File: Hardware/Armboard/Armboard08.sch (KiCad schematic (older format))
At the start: 0 parts

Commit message: Added serial pins, limit switches, titles, and indicators
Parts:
- added Conn? (x3): Molex_SL_03, symbol MRDT_Connectors:Molex_SL_03
- added D? (x6): LED, symbol Device:LED
- added R? (x6): 500, symbol Device:R
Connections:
- new net: D?.2 (A), R?.2 (x6)
- new net GND: Conn?.2, Conn?.2, Conn?.2, D?.1 (K), D?.1 (K), D?.1 (K), D?.1 (K), D?.1 (K), D?.1 (K)
- new net Rx_1_Tiva: Conn?.1, R?.1
- new net Rx_2_Tiva: Conn?.1, R?.1
- new net Rx_3_Tiva: Conn?.1, R?.1
- new net Tx_1_Tiva: Conn?.3, R?.1
- new net Tx_2_Tiva: Conn?.3, R?.1
- new net Tx_3_Tiva: Conn?.3, R?.1
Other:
- note added: "Purple"
- note added: "Serial Pins"

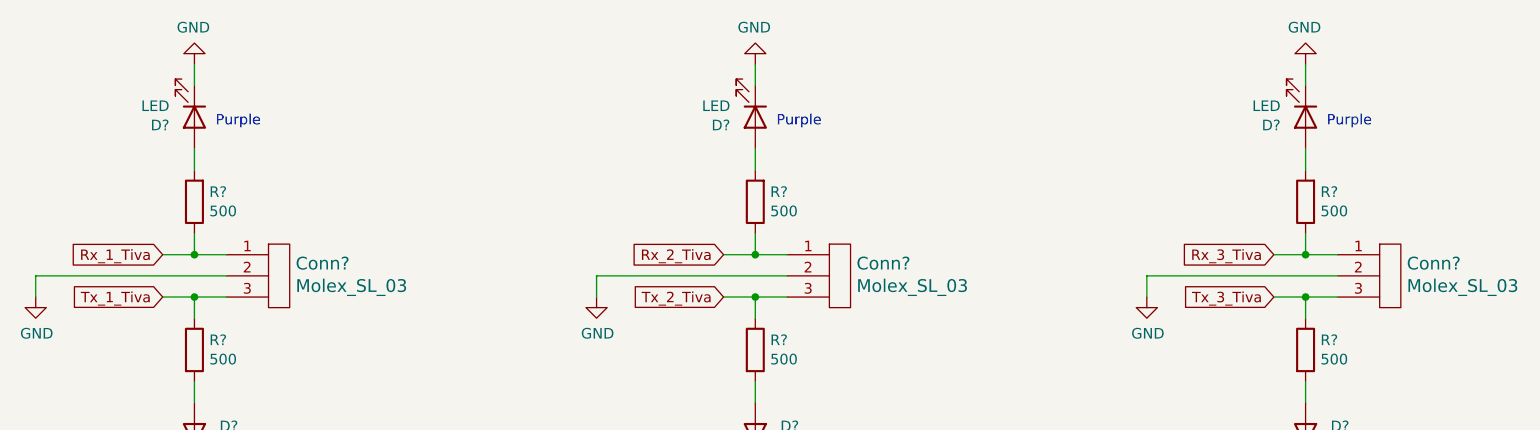
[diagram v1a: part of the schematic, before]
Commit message: Formatted GNDs and added motor toggle buttons
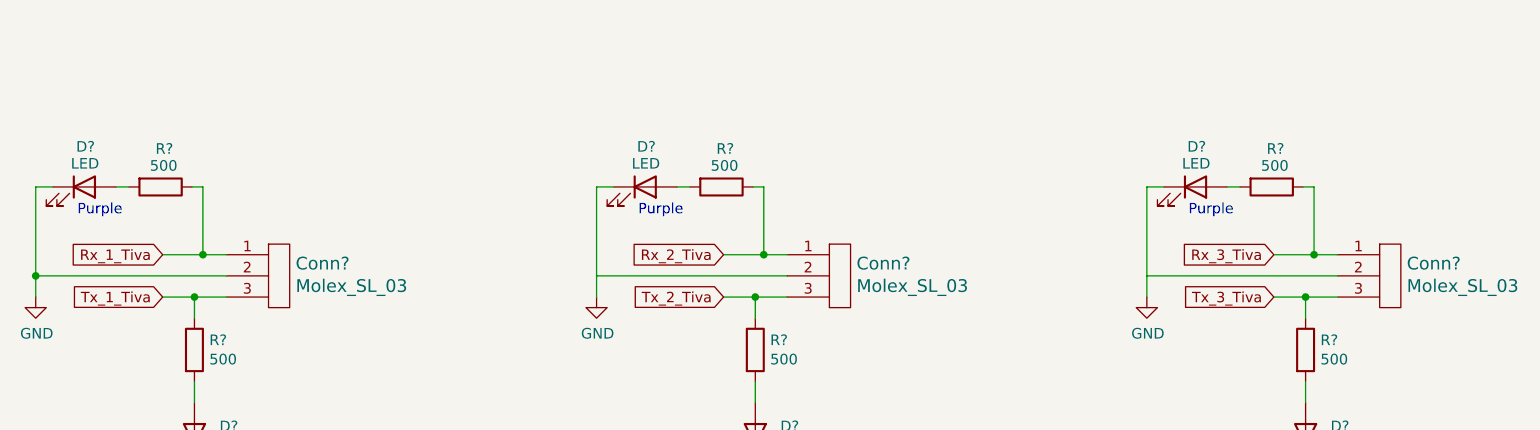
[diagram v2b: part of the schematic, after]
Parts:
- removed D? (x2): LED, symbol Device:LED
- removed R? (x2): 500, symbol Device:R
- added D? (x2): LED, symbol Device:LED
- added R? (x2): 500, symbol Device:R
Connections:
- net GND: now also D?.1 (K), D?.1 (K)
- net Rx_2_Tiva: now also R?.1
- net Rx_3_Tiva: now also R?.1
- new net: D?.2 (A), R?.2 (x2)
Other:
- moved on the sheet: D?, R?
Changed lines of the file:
@@
 Tx_1_Tiva
-Wire Wire Line
-	2950 3550 2800 3550
 Wire Wire Line
 	2950 3750 2800 3750
@@
 L Device:R R?
 U 1 1 5F88CC5B
-P 2800 3300
-F 0 "R?" H 2730 3254 50  0000 R CNN
-F 1 "500" H 2730 3345 50  0000 R CNN
-F 2 "" V 2730 3300 50  0001 C CNN
-F 3 "~" H 2800 3300 50  0001 C CNN
-	1    2800 3300
-	-1   0    0    1
+P 2640 3230
+F 0 "R?" V 2460 3290 50  0000 R CNN
+F 1 "500" V 2540 3310 50  0000 R CNN
+F 2 "" V 2570 3230 50  0001 C CNN
+F 3 "~" H 2640 3230 50  0001 C CNN
+	1    2640 3230
+	0    1    1    0
 $EndComp
 $Comp
 L Device:LED D?
 U 1 1 5F88CC61
-P 2800 2900
-F 0 "D?" V 2839 2782 50  0000 R CNN
-F 1 "LED" V 2748 2782 50  0000 R CNN
-F 2 "" H 2800 2900 50  0001 C CNN
-F 3 "~" H 2800 2900 50  0001 C CNN
-	1    2800 2900
-	0    1    1    0
-$EndComp
-$Comp
-L power:GND #PWR?
-U 1 1 5F88CC67
-P 2800 2650
-F 0 "#PWR?" H 2800 2400 50  0001 C CNN
-F 1 "GND" H 2805 2477 50  0000 C CNN
-F 2 "" H 2800 2650 50  0001 C CNN
-F 3 "" H 2800 2650 50  0001 C CNN
-	1    2800 2650
-	-1   0    0    1
+P 2280 3230
+F 0 "D?" H 2330 3420 50  0000 R CNN
+F 1 "LED" H 2350 3340 50  0000 R CNN
+F 2 "" H 2280 3230 50  0001 C CNN
+F 3 "~" H 2280 3230 50  0001 C CNN
+	1    2280 3230
+	1    0    0    -1
 $EndComp
 Wire Wire Line
@@
 Wire Wire Line
 	2800 4650 2800 4550
-Wire Wire Line
-	2800 3450 2800 3550
-Connection ~ 2800 3550
-Wire Wire Line
-	2800 3550 2650 3550
-Wire Wire Line
-	2800 2750 2800 2650
-Wire Wire Line
-	2800 3050 2800 3150
 Text Notes 2450 4450 0    49   ~ 0
 Purple
-Text Notes 2900 2950 0    49   ~ 0
+Text Notes 2460 3370 2    49   ~ 0
 Purple
 $Comp
@@
 Tx_2_Tiva
 Wire Wire Line
-	5600 3550 5450 3550
-Wire Wire Line
 	5600 3750 5450 3750
 Wire Wire Line
@@
 	1    0    0    -1
 $EndComp
-$Comp
-L Device:R R?
-U 1 1 5F88E69D
-P 5450 3300
-F 0 "R?" H 5380 3254 50  0000 R CNN
-F 1 "500" H 5380 3345 50  0000 R CNN
-F 2 "" V 5380 3300 50  0001 C CNN
-F 3 "~" H 5450 3300 50  0001 C CNN
-	1    5450 3300
-	-1   0    0    1
-$EndComp
-$Comp
-L Device:LED D?
-U 1 1 5F88E6A3
-P 5450 2900
-F 0 "D?" V 5489 2782 50  0000 R CNN
-F 1 "LED" V 5398 2782 50  0000 R CNN
-F 2 "" H 5450 2900 50  0001 C CNN
-F 3 "~" H 5450 2900 50  0001 C CNN
-	1    5450 2900
-	0    1    1    0
-$EndComp
-$Comp
-L power:GND #PWR?
-U 1 1 5F88E6A9
-P 5450 2650
-F 0 "#PWR?" H 5450 2400 50  0001 C CNN
-F 1 "GND" H 5455 2477 50  0000 C CNN
-F 2 "" H 5450 2650 50  0001 C CNN
-F 3 "" H 5450 2650 50  0001 C CNN
-	1    5450 2650
-	-1   0    0    1
-$EndComp
 Wire Wire Line
 	5450 3850 5450 3750
@@
 Wire Wire Line
 	5450 4650 5450 4550
-Wire Wire Line
-	5450 3450 5450 3550
-Connection ~ 5450 3550
-Wire Wire Line
-	5450 3550 5300 3550
-Wire Wire Line
-	5450 2750 5450 2650
-Wire Wire Line
-	5450 3050 5450 3150
 Text Notes 5100 4450 0    49   ~ 0
-Purple
-Text Notes 5550 2950 0    49   ~ 0
 Purple
 $Comp
@@
 Tx_3_Tiva
 Wire Wire Line
-	8200 3550 8050 3550
-Wire Wire Line
 	8200 3750 8050 3750
 Wire Wire Line
@@
 	1    0    0    -1
 $EndComp
-$Comp
-L Device:R R?
-U 1 1 5F88FBD3
-P 8050 3300
-F 0 "R?" H 7980 3254 50  0000 R CNN
-F 1 "500" H 7980 3345 50  0000 R CNN
-F 2 "" V 7980 3300 50  0001 C CNN
-F 3 "~" H 8050 3300 50  0001 C CNN
-	1    8050 3300
-	-1   0    0    1
-$EndComp
-$Comp
-L Device:LED D?
-U 1 1 5F88FBD9
-P 8050 2900
-F 0 "D?" V 8089 2782 50  0000 R CNN
-F 1 "LED" V 7998 2782 50  0000 R CNN
-F 2 "" H 8050 2900 50  0001 C CNN
-F 3 "~" H 8050 2900 50  0001 C CNN
-	1    8050 2900
-	0    1    1    0
-$EndComp
-$Comp
-L power:GND #PWR?
-U 1 1 5F88FBDF
-P 8050 2650
-F 0 "#PWR?" H 8050 2400 50  0001 C CNN
-F 1 "GND" H 8055 2477 50  0000 C CNN
-F 2 "" H 8050 2650 50  0001 C CNN
-F 3 "" H 8050 2650 50  0001 C CNN
-	1    8050 2650
-	-1   0    0    1
-$EndComp
 Wire Wire Line
 	8050 3850 8050 3750
@@
 Wire Wire Line
 	8050 4650 8050 4550
-Wire Wire Line
-	8050 3450 8050 3550
-Connection ~ 8050 3550
-Wire Wire Line
-	8050 3550 7900 3550
-Wire Wire Line
-	8050 2750 8050 2650
-Wire Wire Line
-	8050 3050 8050 3150
 Text Notes 7700 4450 0    49   ~ 0
 Purple
-Text Notes 8150 2950 0    49   ~ 0
-Purple
+Wire Wire Line
+	2650 3550 2840 3550
+Wire Wire Line
+	2050 3650 2050 3230
+Connection ~ 2050 3650
+Wire Wire Line
+	2050 3230 2130 3230
+Wire Wire Line
+	2430 3230 2490 3230
+Wire Wire Line
+	2790 3230 2840 3230
+Wire Wire Line
+	2840 3230 2840 3550
+Connection ~ 2840 3550
+Wire Wire Line
+	2840 3550 2950 3550
+Wire Wire Line
+	5300 3550 5490 3550
+$Comp
+L Device:R R?
+U 1 1 5F8577E4
+P 5290 3230
+F 0 "R?" V 5110 3290 50  0000 R CNN
+F 1 "500" V 5190 3310 50  0000 R CNN
+F 2 "" V 5220 3230 50  0001 C CNN
+F 3 "~" H 5290 3230 50  0001 C CNN
+	1    5290 3230
+	0    1    1    0
+$EndComp
+$Comp
+L Device:LED D?
+U 1 1 5F8577EA
+P 4930 3230
+F 0 "D?" H 4980 3420 50  0000 R CNN
+F 1 "LED" H 5000 3340 50  0000 R CNN
+F 2 "" H 4930 3230 50  0001 C CNN
+F 3 "~" H 4930 3230 50  0001 C CNN
+	1    4930 3230
+	1    0    0    -1
+$EndComp
+Text Notes 5110 3370 2    49   ~ 0
+Purple
+Wire Wire Line
+	4700 3650 4700 3230
+Wire Wire Line
+	4700 3230 4780 3230
+Wire Wire Line
+	5080 3230 5140 3230
+Wire Wire Line
+	5440 3230 5490 3230
+Wire Wire Line
+	7900 3550 8090 3550
+$Comp
+L Device:R R?
+U 1 1 5F858A89
+P 7890 3230
+F 0 "R?" V 7710 3290 50  0000 R CNN
+F 1 "500" V 7790 3310 50  0000 R CNN
+F 2 "" V 7820 3230 50  0001 C CNN
+F 3 "~" H 7890 3230 50  0001 C CNN
+	1    7890 3230
+	0    1    1    0
+$EndComp
+$Comp
+L Device:LED D?
+U 1 1 5F858A8F
+P 7530 3230
+F 0 "D?" H 7580 3420 50  0000 R CNN
+F 1 "LED" H 7600 3340 50  0000 R CNN
+F 2 "" H 7530 3230 50  0001 C CNN
+F 3 "~" H 7530 3230 50  0001 C CNN
+	1    7530 3230
+	1    0    0    -1
+$EndComp
+Text Notes 7710 3370 2    49   ~ 0
+Purple
+Wire Wire Line
+	7300 3650 7300 3230
+Wire Wire Line
+	7300 3230 7380 3230
+Wire Wire Line
+	7680 3230 7740 3230
+Wire Wire Line
+	8040 3230 8090 3230
+Wire Wire Line
+	8090 3230 8090 3550
+Connection ~ 8090 3550
+Wire Wire Line
+	8090 3550 8200 3550
+Wire Wire Line
+	5490 3230 5490 3550
+Connection ~ 5490 3550
+Wire Wire Line
+	5490 3550 5600 3550
 $EndSCHEMATC

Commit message: Fixed buttons/switches page, changed resistor values, fixed some tiva connections
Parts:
- removed D? (x3): LED, symbol Device:LED
- removed R? (x3): 500, symbol Device:R
- added D? (x3): LED, symbol Device:LED
- added R? (x3): 330, symbol Device:R
- R? (x3): value 500 -> 330
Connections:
- net GND: now also D?.1 (K), D?.1 (K), D?.1 (K)
- net Rx_1_Tiva: now also R?.2
- net Rx_2_Tiva: now also R?.2
- net Rx_3_Tiva: now also R?.2
- new net: D?.2 (A), R?.1 (x3)
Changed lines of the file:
@@
 Text GLabel 2650 3550 0    49   Input ~ 0
 Rx_1_Tiva
-Text GLabel 2650 3750 0    49   Input ~ 0
+Text GLabel 2650 3750 0    49   Output ~ 0
 Tx_1_Tiva
 Wire Wire Line
@@
 P 2800 4000
 F 0 "R?" H 2870 4046 50  0000 L CNN
-F 1 "500" H 2870 3955 50  0000 L CNN
+F 1 "330" H 2870 3955 50  0000 L CNN
 F 2 "" V 2730 4000 50  0001 C CNN
 F 3 "~" H 2800 4000 50  0001 C CNN
@@
 	1    0    0    -1
 $EndComp
-$Comp
-L Device:R R?
-U 1 1 5F88CC5B
-P 2640 3230
-F 0 "R?" V 2460 3290 50  0000 R CNN
-F 1 "500" V 2540 3310 50  0000 R CNN
-F 2 "" V 2570 3230 50  0001 C CNN
-F 3 "~" H 2640 3230 50  0001 C CNN
-	1    2640 3230
-	0    1    1    0
-$EndComp
-$Comp
-L Device:LED D?
-U 1 1 5F88CC61
-P 2280 3230
-F 0 "D?" H 2330 3420 50  0000 R CNN
-F 1 "LED" H 2350 3340 50  0000 R CNN
-F 2 "" H 2280 3230 50  0001 C CNN
-F 3 "~" H 2280 3230 50  0001 C CNN
-	1    2280 3230
-	1    0    0    -1
-$EndComp
 Wire Wire Line
 	2800 3850 2800 3750
@@
 	2800 4650 2800 4550
 Text Notes 2450 4450 0    49   ~ 0
-Purple
-Text Notes 2460 3370 2    49   ~ 0
 Purple
 $Comp
@@
 Text GLabel 5300 3550 0    49   Input ~ 0
 Rx_2_Tiva
-Text GLabel 5300 3750 0    49   Input ~ 0
+Text GLabel 5300 3750 0    49   Output ~ 0
 Tx_2_Tiva
 Wire Wire Line
@@
 P 5450 4000
 F 0 "R?" H 5520 4046 50  0000 L CNN
-F 1 "500" H 5520 3955 50  0000 L CNN
+F 1 "330" H 5520 3955 50  0000 L CNN
 F 2 "" V 5380 4000 50  0001 C CNN
 F 3 "~" H 5450 4000 50  0001 C CNN
@@
 Text GLabel 7900 3550 0    49   Input ~ 0
 Rx_3_Tiva
-Text GLabel 7900 3750 0    49   Input ~ 0
+Text GLabel 7900 3750 0    49   Output ~ 0
 Tx_3_Tiva
 Wire Wire Line
@@
 P 8050 4000
 F 0 "R?" H 8120 4046 50  0000 L CNN
-F 1 "500" H 8120 3955 50  0000 L CNN
+F 1 "330" H 8120 3955 50  0000 L CNN
 F 2 "" V 7980 4000 50  0001 C CNN
 F 3 "~" H 8050 4000 50  0001 C CNN
@@
 Text Notes 7700 4450 0    49   ~ 0
 Purple
-Wire Wire Line
-	2650 3550 2840 3550
-Wire Wire Line
-	2050 3650 2050 3230
-Connection ~ 2050 3650
-Wire Wire Line
-	2050 3230 2130 3230
-Wire Wire Line
-	2430 3230 2490 3230
-Wire Wire Line
-	2790 3230 2840 3230
-Wire Wire Line
-	2840 3230 2840 3550
-Connection ~ 2840 3550
-Wire Wire Line
-	2840 3550 2950 3550
-Wire Wire Line
-	5300 3550 5490 3550
-$Comp
-L Device:R R?
-U 1 1 5F8577E4
-P 5290 3230
-F 0 "R?" V 5110 3290 50  0000 R CNN
-F 1 "500" V 5190 3310 50  0000 R CNN
-F 2 "" V 5220 3230 50  0001 C CNN
-F 3 "~" H 5290 3230 50  0001 C CNN
-	1    5290 3230
+Text Notes 2705 2920 2    49   ~ 0
+Purple
+$Comp
+L Device:LED D?
+U 1 1 5F972EFB
+P 2800 2895
+F 0 "D?" V 2747 2975 50  0000 L CNN
+F 1 "LED" V 2838 2975 50  0000 L CNN
+F 2 "" H 2800 2895 50  0001 C CNN
+F 3 "~" H 2800 2895 50  0001 C CNN
+	1    2800 2895
 	0    1    1    0
 $EndComp
 $Comp
-L Device:LED D?
-U 1 1 5F8577EA
-P 4930 3230
-F 0 "D?" H 4980 3420 50  0000 R CNN
-F 1 "LED" H 5000 3340 50  0000 R CNN
-F 2 "" H 4930 3230 50  0001 C CNN
-F 3 "~" H 4930 3230 50  0001 C CNN
-	1    4930 3230
-	1    0    0    -1
-$EndComp
-Text Notes 5110 3370 2    49   ~ 0
-Purple
-Wire Wire Line
-	4700 3650 4700 3230
-Wire Wire Line
-	4700 3230 4780 3230
-Wire Wire Line
-	5080 3230 5140 3230
-Wire Wire Line
-	5440 3230 5490 3230
-Wire Wire Line
-	7900 3550 8090 3550
-$Comp
-L Device:R R?
-U 1 1 5F858A89
-P 7890 3230
-F 0 "R?" V 7710 3290 50  0000 R CNN
-F 1 "500" V 7790 3310 50  0000 R CNN
-F 2 "" V 7820 3230 50  0001 C CNN
-F 3 "~" H 7890 3230 50  0001 C CNN
-	1    7890 3230
+L Device:R R?
+U 1 1 5F973771
+P 2800 3285
+F 0 "R?" H 2870 3331 50  0000 L CNN
+F 1 "330" H 2870 3240 50  0000 L CNN
+F 2 "" V 2730 3285 50  0001 C CNN
+F 3 "~" H 2800 3285 50  0001 C CNN
+	1    2800 3285
+	1    0    0    -1
+$EndComp
+$Comp
+L power:GND #PWR?
+U 1 1 5F9742DF
+P 3120 2585
+F 0 "#PWR?" H 3120 2335 50  0001 C CNN
+F 1 "GND" H 3125 2412 50  0000 C CNN
+F 2 "" H 3120 2585 50  0001 C CNN
+F 3 "" H 3120 2585 50  0001 C CNN
+	1    3120 2585
+	1    0    0    -1
+$EndComp
+Wire Wire Line
+	2800 3135 2800 3045
+Wire Wire Line
+	2800 2745 2800 2530
+Wire Wire Line
+	3120 2530 3120 2585
+Wire Wire Line
+	2800 2530 3120 2530
+Wire Wire Line
+	2650 3550 2800 3550
+Wire Wire Line
+	2800 3435 2800 3550
+Connection ~ 2800 3550
+Wire Wire Line
+	2800 3550 2950 3550
+Wire Wire Line
+	5300 3550 5450 3550
+Wire Wire Line
+	7900 3550 8050 3550
+Text Notes 7955 2915 2    49   ~ 0
+Purple
+$Comp
+L Device:LED D?
+U 1 1 5F97D8E9
+P 8050 2890
+F 0 "D?" V 7997 2970 50  0000 L CNN
+F 1 "LED" V 8088 2970 50  0000 L CNN
+F 2 "" H 8050 2890 50  0001 C CNN
+F 3 "~" H 8050 2890 50  0001 C CNN
+	1    8050 2890
 	0    1    1    0
 $EndComp
 $Comp
-L Device:LED D?
-U 1 1 5F858A8F
-P 7530 3230
-F 0 "D?" H 7580 3420 50  0000 R CNN
-F 1 "LED" H 7600 3340 50  0000 R CNN
-F 2 "" H 7530 3230 50  0001 C CNN
-F 3 "~" H 7530 3230 50  0001 C CNN
-	1    7530 3230
-	1    0    0    -1
-$EndComp
-Text Notes 7710 3370 2    49   ~ 0
-Purple
-Wire Wire Line
-	7300 3650 7300 3230
-Wire Wire Line
-	7300 3230 7380 3230
-Wire Wire Line
-	7680 3230 7740 3230
-Wire Wire Line
-	8040 3230 8090 3230
-Wire Wire Line
-	8090 3230 8090 3550
-Connection ~ 8090 3550
-Wire Wire Line
-	8090 3550 8200 3550
-Wire Wire Line
-	5490 3230 5490 3550
-Connection ~ 5490 3550
-Wire Wire Line
-	5490 3550 5600 3550
+L Device:R R?
+U 1 1 5F97D8EF
+P 8050 3280
+F 0 "R?" H 8120 3326 50  0000 L CNN
+F 1 "330" H 8120 3235 50  0000 L CNN
+F 2 "" V 7980 3280 50  0001 C CNN
+F 3 "~" H 8050 3280 50  0001 C CNN
+	1    8050 3280
+	1    0    0    -1
+$EndComp
+$Comp
+L power:GND #PWR?
+U 1 1 5F97D8F5
+P 8370 2580
+F 0 "#PWR?" H 8370 2330 50  0001 C CNN
+F 1 "GND" H 8375 2407 50  0000 C CNN
+F 2 "" H 8370 2580 50  0001 C CNN
+F 3 "" H 8370 2580 50  0001 C CNN
+	1    8370 2580
+	1    0    0    -1
+$EndComp
+Wire Wire Line
+	8050 3130 8050 3040
+Wire Wire Line
+	8050 2740 8050 2525
+Wire Wire Line
+	8370 2525 8370 2580
+Wire Wire Line
+	8050 2525 8370 2525
+Wire Wire Line
+	5450 2530 5770 2530
+Wire Wire Line
+	5770 2530 5770 2585
+Wire Wire Line
+	5450 2745 5450 2530
+Wire Wire Line
+	5450 3135 5450 3045
+$Comp
+L power:GND #PWR?
+U 1 1 5F97CA71
+P 5770 2585
+F 0 "#PWR?" H 5770 2335 50  0001 C CNN
+F 1 "GND" H 5775 2412 50  0000 C CNN
+F 2 "" H 5770 2585 50  0001 C CNN
+F 3 "" H 5770 2585 50  0001 C CNN
+	1    5770 2585
+	1    0    0    -1
+$EndComp
+$Comp
+L Device:R R?
+U 1 1 5F97CA6B
+P 5450 3285
+F 0 "R?" H 5520 3331 50  0000 L CNN
+F 1 "330" H 5520 3240 50  0000 L CNN
+F 2 "" V 5380 3285 50  0001 C CNN
+F 3 "~" H 5450 3285 50  0001 C CNN
+	1    5450 3285
+	1    0    0    -1
+$EndComp
+$Comp
+L Device:LED D?
+U 1 1 5F97CA65
+P 5450 2895
+F 0 "D?" V 5397 2975 50  0000 L CNN
+F 1 "LED" V 5488 2975 50  0000 L CNN
+F 2 "" H 5450 2895 50  0001 C CNN
+F 3 "~" H 5450 2895 50  0001 C CNN
+	1    5450 2895
+	0    1    1    0
+$EndComp
+Text Notes 5355 2920 2    49   ~ 0
+Purple
+Wire Wire Line
+	5450 3435 5450 3550
+Connection ~ 5450 3550
+Wire Wire Line
+	5450 3550 5600 3550
+Wire Wire Line
+	8050 3430 8050 3550
+Connection ~ 8050 3550
+Wire Wire Line
+	8050 3550 8200 3550
 $EndSCHEMATC
